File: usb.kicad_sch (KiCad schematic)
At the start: 34 parts, among them J1 USB_C_Receptacle_USB2.0, Q1 AO4805, Q2 AO4805, Q3 DMG2302U, U1 USBLC6-2SC6, U2 CYPD3177-24LQXQ

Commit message: WIP PCB routing
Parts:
- C1: footprint Capacitor_SMD:C_0603_1608Metric -> Capacitor_SMD:C_1210_3225Metric
- U2: footprint Package_DFN_QFN:QFN-24-1EP_4x4mm_P0.5mm_EP2.7x2.7mm_ThermalVias -> Package_DFN_QFN:QFN-24-1EP_4x4mm_P0.5mm_EP2.7x2.7mm
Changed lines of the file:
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@@
       (effects (font (size 1.27 1.27)) (justify left))
     )
-    (property "Footprint" "Package_DFN_QFN:QFN-24-1EP_4x4mm_P0.5mm_EP2.7x2.7mm_ThermalVias" (id 2) (at 212.09 129.54 0)
+    (property "Footprint" "Package_DFN_QFN:QFN-24-1EP_4x4mm_P0.5mm_EP2.7x2.7mm" (id 2) (at 212.09 129.54 0)
       (effects (font (size 1.27 1.27)) hide)
     )
@@
       (effects (font (size 1.27 1.27)) (justify left))
     )
-    (property "Footprint" "Capacitor_SMD:C_0603_1608Metric" (id 2) (at 133.35 50.8 0)
+    (property "Footprint" "Capacitor_SMD:C_1210_3225Metric" (id 2) (at 133.35 50.8 0)
       (effects (font (size 1.27 1.27)) hide)
     )

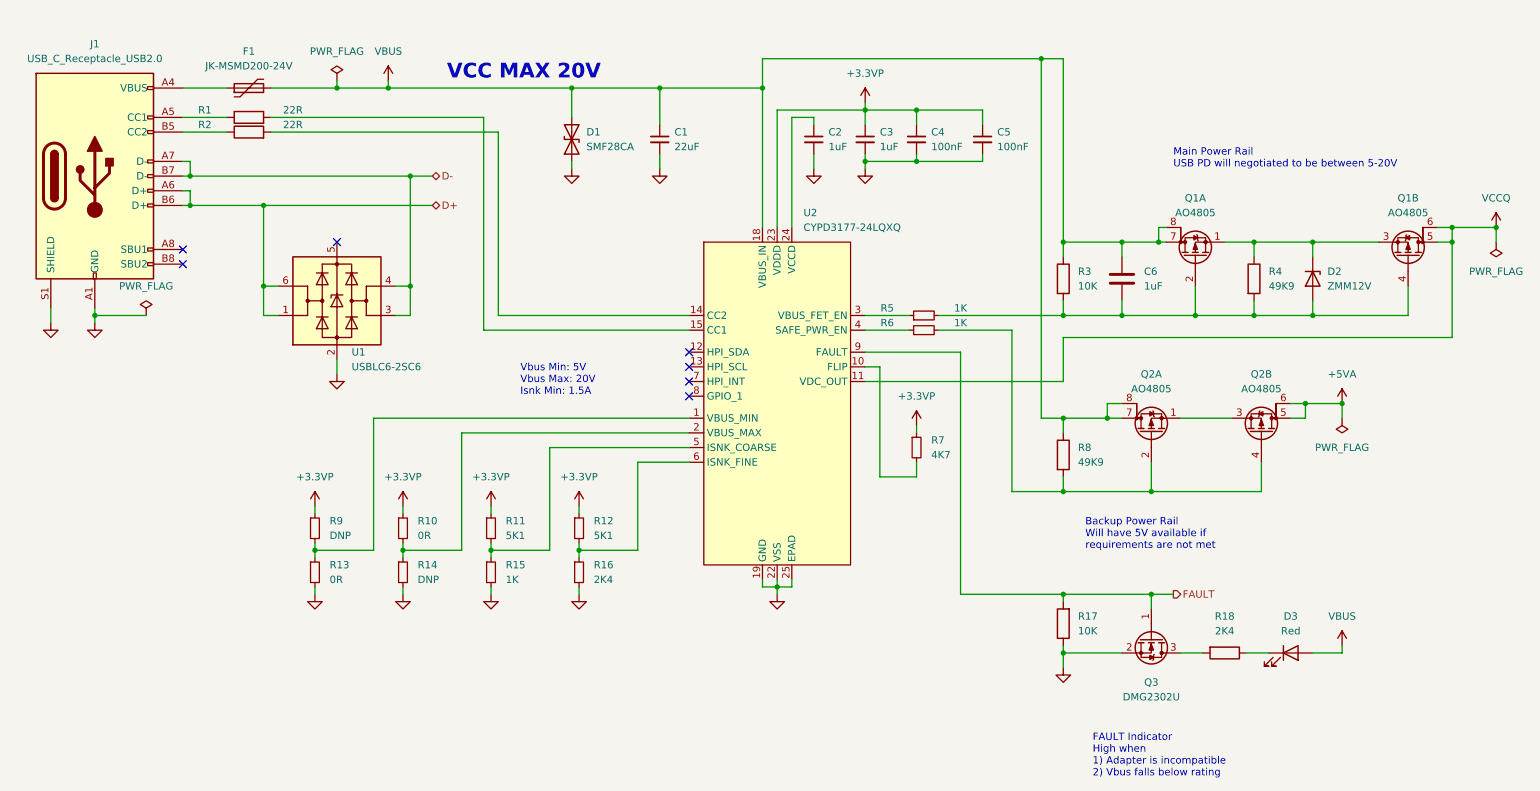
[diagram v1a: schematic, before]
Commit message: Add information and BOM consolidation for JLCPCB
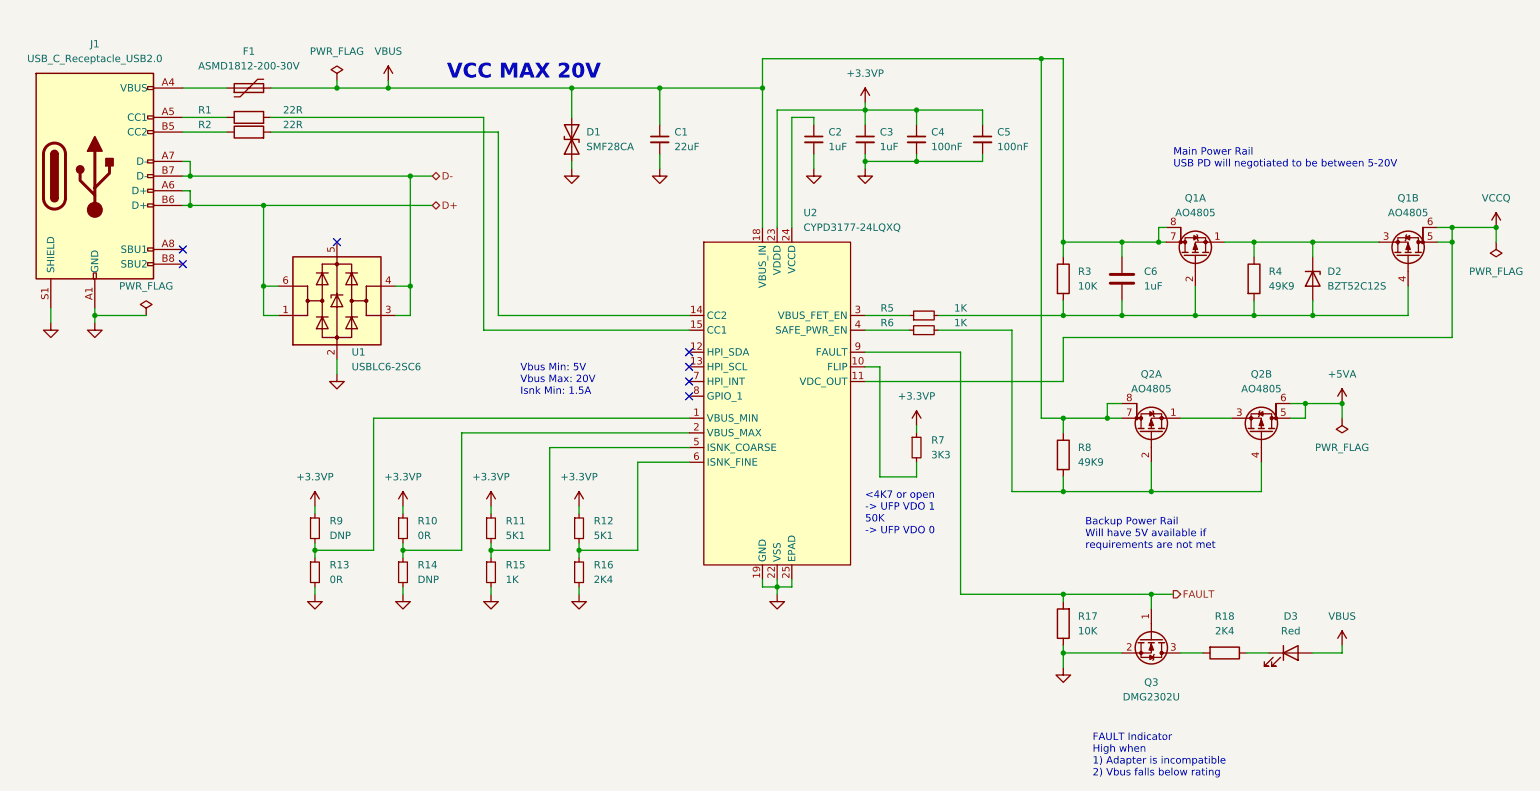
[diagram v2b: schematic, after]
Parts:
- D2: value ZMM12V -> BZT52C12S
- F1: value JK-MSMD200-24V -> ASMD1812-200-30V
- R7: value 4K7 -> 3K3
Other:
- note added: "<4K7 or open -> UFP VDO 1 50K -> UFP VDO 0"
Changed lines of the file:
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@@
     (effects (font (size 2.54 2.54) (thickness 0.508) bold) (justify left bottom))
+  )
+  (text "<4K7 or open\n-> UFP VDO 1\n50K\n-> UFP VDO 0" (at 168.91 119.38 0)
+    (effects (font (size 1.27 1.27)) (justify left bottom))
   )
   (text "FAULT Indicator\nHigh when\n1) Adapter is incompatible\n2) Vbus falls below rating"
@@
     (in_bom yes) (on_board yes) (fields_autoplaced)
     (property "Reference" "F1" (id 0) (at 62.23 35.56 90))
-    (property "Value" "JK-MSMD200-24V" (id 1) (at 62.23 38.1 90))
+    (property "Value" "ASMD1812-200-30V" (id 1) (at 62.23 38.1 90))
     (property "Footprint" "Fuse:Fuse_1812_4532Metric" (id 2) (at 67.31 40.64 0)
       (effects (font (size 1.27 1.27)) (justify left) hide)
@@
       (effects (font (size 1.27 1.27)) (justify left))
     )
-    (property "Value" "4K7" (id 1) (at 180.34 105.4099 0)
+    (property "Value" "3K3" (id 1) (at 180.34 105.4099 0)
       (effects (font (size 1.27 1.27)) (justify left))
     )
@@
       (effects (font (size 1.27 1.27)) (justify left))
     )
-    (property "Value" "ZMM12V" (id 1) (at 248.92 76.1999 90)
-      (effects (font (size 1.27 1.27)) (justify left))
-    )
+    (property "Value" "BZT52C12S" (id 1) (at 248.92 76.1999 90)
+      (effects (font (size 1.27 1.27)) (justify left))
+    )

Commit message: Power optimization, add Aisler Assembly MPN info
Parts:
- C1: MPN (none) -> 22uF 25V X7R
- C2, C3, C6: MPN (none) -> 1uF 50V X7R
- C4, C5: MPN (none) -> 100nF 50V X7R
- D1: MPN (none) -> SMF28CA
- D2: MPN (none) -> BZT52C12S
- D3: MPN (none) -> KT-0603R
- F1: MPN (none) -> ASMD1812-200-30V
- J1: MPN (none) -> HC-TYPE-C-16P-01A
- Q1, Q2: MPN (none) -> AO4805
- Q3: value DMG2302U -> SI2302
- R1, R2: MPN (none) -> 22R 1%
- R10, R13: MPN (none) -> 0R 1%
- R11, R12: MPN (none) -> 5K1 1%
- R15, R5, R6: MPN (none) -> 1K 1%
- R16, R18: MPN (none) -> 2K4 1%
- R17, R3: MPN (none) -> 10K 1%
- R4, R8: MPN (none) -> 49K9 1%
- R7: MPN (none) -> 3K3 1%
- U1: MPN (none) -> USBLC6-2SC6
- U2: MPN (none) -> CYPD3177-24LQXQ
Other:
- note added: "4A Fuse Max 80W"
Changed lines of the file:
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@@
+    (effects (font (size 1.27 1.27)) (justify left bottom))
+  )
+  (text "4A Fuse\nMax 80W" (at 58.42 33.02 0)
     (effects (font (size 1.27 1.27)) (justify left bottom))
   )
@@
     )
     (property "Datasheet" "~" (id 3) (at 262.89 69.85 0)
+      (effects (font (size 1.27 1.27)) hide)
+    )
+    (property "MPN" "AO4805" (id 4) (at 226.06 71.12 0)
       (effects (font (size 1.27 1.27)) hide)
     )
@@
     )
     (property "Datasheet" "https://datasheet.lcsc.com/lcsc/2208051100_Cypress-Semicon-CYPD3177-24LQXQ_C2959321.pdf" (id 3) (at 210.82 132.08 0)
+      (effects (font (size 1.27 1.27)) hide)
+    )
+    (property "MPN" "CYPD3177-24LQXQ" (id 4) (at 153.67 96.52 0)
       (effects (font (size 1.27 1.27)) hide)
     )
@@
       (effects (font (size 1.27 1.27)) hide)
     )
+    (property "MPN" "100nF 50V X7R" (id 4) (at 189.23 50.8 0)
+      (effects (font (size 1.27 1.27)) hide)
+    )
     (pin "1")
     (pin "2")
@@
       (effects (font (size 1.27 1.27)) hide)
     )
+    (property "MPN" "100nF 50V X7R" (id 4) (at 177.8 50.8 0)
+      (effects (font (size 1.27 1.27)) hide)
+    )
     (pin "1")
     (pin "2")
@@
     )
     (property "Datasheet" "~" (id 3) (at 88.9 118.11 0)
+      (effects (font (size 1.27 1.27)) hide)
+    )
+    (property "MPN" "0R 1%" (id 4) (at 88.9 118.11 0)
       (effects (font (size 1.27 1.27)) hide)
     )
@@
     )
     (property "Datasheet" "~" (id 3) (at 237.49 100.33 0)
+      (effects (font (size 1.27 1.27)) hide)
+    )
+    (property "MPN" "AO4805" (id 4) (at 218.44 101.6 0)
       (effects (font (size 1.27 1.27)) hide)
     )
@@
       (effects (font (size 1.27 1.27)) hide)
     )
+    (property "MPN" "22uF 25V X7R" (id 4) (at 133.35 50.8 0)
+      (effects (font (size 1.27 1.27)) hide)
+    )
     (pin "1")
     (pin "2")
@@
       (effects (font (size 1.27 1.27)) hide)
     )
+    (property "MPN" "2K4 1%" (id 4) (at 119.38 125.73 0)
+      (effects (font (size 1.27 1.27)) hide)
+    )
     (pin "1")
     (pin "2")
@@
     )
     (property "Datasheet" "~" (id 3) (at 203.2 134.62 0)
+      (effects (font (size 1.27 1.27)) hide)
+    )
+    (property "MPN" "10K 1%" (id 4) (at 203.2 134.62 0)
       (effects (font (size 1.27 1.27)) hide)
     )
@@
     )
     (property "Datasheet" "~" (id 3) (at 218.44 100.33 0)
+      (effects (font (size 1.27 1.27)) hide)
+    )
+    (property "MPN" "AO4805" (id 4) (at 218.44 101.6 0)
       (effects (font (size 1.27 1.27)) hide)
     )
@@
       (effects (font (size 1.27 1.27)) hide)
     )
+    (property "MPN" "1uF 50V X7R" (id 4) (at 160.02 50.8 0)
+      (effects (font (size 1.27 1.27)) hide)
+    )
     (pin "1")
     (pin "2")
@@
     )
     (property "Datasheet" "~" (id 3) (at 168.91 50.8 0)
+      (effects (font (size 1.27 1.27)) hide)
+    )
+    (property "MPN" "1uF 50V X7R" (id 4) (at 168.91 50.8 0)
       (effects (font (size 1.27 1.27)) hide)
     )
@@
     )
     (property "Datasheet" "~" (id 3) (at 213.36 74.93 0)
+      (effects (font (size 1.27 1.27)) hide)
+    )
+    (property "MPN" "1uF 50V X7R" (id 4) (at 213.36 74.93 0)
       (effects (font (size 1.27 1.27)) hide)
     )
@@
       (effects (font (size 1.27 1.27)) hide)
     )
+    (property "MPN" "KT-0603R" (id 4) (at 242.57 139.7 0)
+      (effects (font (size 1.27 1.27)) hide)
+    )
     (pin "1")
     (pin "2")
@@
       (effects (font (size 1.27 1.27)) hide)
     )
+    (property "MPN" "22R 1%" (id 4) (at 62.23 46.99 0)
+      (effects (font (size 1.27 1.27)) hide)
+    )
     (pin "1")
     (pin "2")
@@
       (effects (font (size 1.27 1.27)) hide)
     )
+    (property "MPN" "ASMD1812-200-30V" (id 4) (at 62.23 41.91 0)
+      (effects (font (size 1.27 1.27)) hide)
+    )
     (pin "1")
     (pin "2")
@@
       (effects (font (size 1.27 1.27)) hide)
     )
+    (property "MPN" "1K 1%" (id 4) (at 104.14 125.73 0)
+      (effects (font (size 1.27 1.27)) hide)
+    )
     (pin "1")
     (pin "2")
@@
       (effects (font (size 1.27 1.27)) hide)
     )
+    (property "MPN" "49K9 1%" (id 4) (at 236.22 74.93 0)
+      (effects (font (size 1.27 1.27)) hide)
+    )
     (pin "1")
     (pin "2")
@@
     )
     (property "Datasheet" "~" (id 3) (at 104.14 118.11 0)
+      (effects (font (size 1.27 1.27)) hide)
+    )
+    (property "MPN" "5K1 1%" (id 4) (at 104.14 118.11 0)
       (effects (font (size 1.27 1.27)) hide)
     )
@@
     )
     (property "Datasheet" "https://www.usb.org/sites/default/files/documents/usb_type-c.zip" (id 3) (at 39.37 57.15 0)
+      (effects (font (size 1.27 1.27)) hide)
+    )
+    (property "MPN" "HC-TYPE-C-16P-01A" (id 4) (at 35.56 57.15 0)
       (effects (font (size 1.27 1.27)) hide)
     )
@@
       (effects (font (size 1.27 1.27)) hide)
     )
+    (property "MPN" "1K 1%" (id 4) (at 179.07 81.28 0)
+      (effects (font (size 1.27 1.27)) hide)
+    )
     (pin "1")
     (pin "2")
@@
       (effects (font (size 1.27 1.27)) hide)
     )
+    (property "MPN" "2K4 1%" (id 4) (at 231.14 139.7 0)
+      (effects (font (size 1.27 1.27)) hide)
+    )
     (pin "1")
     (pin "2")
@@
     )
     (property "Datasheet" "~" (id 3) (at 226.06 69.85 0)
+      (effects (font (size 1.27 1.27)) hide)
+    )
+    (property "MPN" "AO4805" (id 4) (at 226.06 71.12 0)
       (effects (font (size 1.27 1.27)) hide)
     )
@@
       (effects (font (size 1.27 1.27)) hide)
     )
+    (property "MPN" "SMF28CA" (id 4) (at 118.11 50.8 0)
+      (effects (font (size 1.27 1.27)) hide)
+    )
     (pin "1")
     (pin "2")
@@
       (effects (font (size 1.27 1.27)) hide)
     )
+    (property "MPN" "10K 1%" (id 4) (at 203.2 74.93 0)
+      (effects (font (size 1.27 1.27)) hide)
+    )
     (pin "1")
     (pin "2")
@@
       (effects (font (size 1.27 1.27)) hide)
     )
+    (property "MPN" "5K1 1%" (id 4) (at 119.38 118.11 0)
+      (effects (font (size 1.27 1.27)) hide)
+    )
     (pin "1")
     (pin "2")
@@
     )
     (property "Datasheet" "~" (id 3) (at 203.2 105.41 0)
+      (effects (font (size 1.27 1.27)) hide)
+    )
+    (property "MPN" "49K9 1%" (id 4) (at 203.2 105.41 0)
       (effects (font (size 1.27 1.27)) hide)
     )
@@
       (effects (font (size 1.27 1.27)) hide)
     )
+    (property "MPN" "22R 1%" (id 4) (at 62.23 49.53 0)
+      (effects (font (size 1.27 1.27)) hide)
+    )
     (pin "1")
     (pin "2")
@@
     )
     (property "Datasheet" "~" (id 3) (at 73.66 125.73 0)
+      (effects (font (size 1.27 1.27)) hide)
+    )
+    (property "MPN" "0R 1%" (id 4) (at 73.66 125.73 0)
       (effects (font (size 1.27 1.27)) hide)
     )
@@
     (in_bom yes) (on_board yes) (fields_autoplaced)
     (property "Reference" "Q3" (id 0) (at 218.44 144.78 90))
-    (property "Value" "DMG2302U" (id 1) (at 218.44 147.32 90))
+    (property "Value" "SI2302" (id 1) (at 218.44 147.32 90))
     (property "Footprint" "Package_TO_SOT_SMD:SOT-23" (id 2) (at 216.535 142.24 0)
       (effects (font (size 1.27 1.27) italic) (justify left) hide)
@@
     )
     (property "Datasheet" "~" (id 3) (at 177.8 104.14 0)
+      (effects (font (size 1.27 1.27)) hide)
+    )
+    (property "MPN" "3K3 1%" (id 4) (at 177.8 104.14 0)
       (effects (font (size 1.27 1.27)) hide)
     )
@@
       (effects (font (size 1.27 1.27)) hide)
     )
+    (property "MPN" "1K 1%" (id 4) (at 179.07 83.82 0)
+      (effects (font (size 1.27 1.27)) hide)
+    )
     (pin "1")
     (pin "2")
@@
     )
     (property "Datasheet" "~" (id 3) (at 246.38 74.93 0)
+      (effects (font (size 1.27 1.27)) hide)
+    )
+    (property "MPN" "BZT52C12S" (id 4) (at 246.38 74.93 0)
       (effects (font (size 1.27 1.27)) hide)
     )
@@
       (effects (font (size 1.27 1.27)) hide)
     )
+    (property "MPN" "USBLC6-2SC6" (id 4) (at 77.47 78.74 0)
+      (effects (font (size 1.27 1.27)) hide)
+    )

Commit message: Create IBOM, Add sheet info
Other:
- company: (none) -> Sleepy Pony Labs
- title: (none) -> Dual Rail Breadboard Power Supply
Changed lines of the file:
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@@
 (kicad_sch (version 20211123) (generator eeschema)
   (paper "A4")
+  (title_block
+    (title "Dual Rail Breadboard Power Supply")
+    (date "2023-06-11")
+    (rev "1")
+    (company "Sleepy Pony Labs")
+  )
   (junction (at 219.71 68.58) (diameter 0) (color 0 0 0 0)
   )

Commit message: Fixed R7 value
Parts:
- R7: value 3K3 -> 2K4
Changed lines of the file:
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@@
       (effects (font (size 1.27 1.27)) (justify left))
     )
-    (property "Value" "3K3" (id 1) (at 180.34 105.4099 0)
+    (property "Value" "2K4" (id 1) (at 180.34 105.4099 0)
       (effects (font (size 1.27 1.27)) (justify left))
     )
